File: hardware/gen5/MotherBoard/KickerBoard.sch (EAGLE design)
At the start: 154 parts, among them U1 SAM3S4B

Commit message: More Motherboard layout progress
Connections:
- removed net M0QA: U1.PA30
- removed net M0QB: U1.PA29
- removed net M1QA: U1.PA27
- removed net M1QB: U1.PA28
- removed net M2QA: U1.PA25
- removed net M2QB: U1.PA26
- removed net M3QA: U1.PA31
- removed net M3QB: U1.PA24
- net M1QA-1: now also U1.PA25
- net M1QA-2: now also U1.PA27
- net M1QA-3: now also U1.PA30
- net M1QA-4: now also U1.PA31
- net M1QB-1: now also U1.PA26
- net M1QB-2: now also U1.PA28
- net M1QB-3: now also U1.PA29
- net M1QB-4: now also U1.PA24
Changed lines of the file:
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@@
 <label x="495.3" y="137.16" size="1.778" layer="95"/>
+</segment>
+<segment>
+<pinref part="U1" gate="G$1" pin="PA24"/>
+<wire x1="746.76" y1="68.58" x2="746.76" y2="30.48" width="0.1524" layer="91"/>
+<label x="746.76" y="30.48" size="1.778" layer="95" rot="R90"/>
 </segment>
 </net>
@@
 <label x="495.3" y="142.24" size="1.778" layer="95"/>
 </segment>
+<segment>
+<pinref part="U1" gate="G$1" pin="PA31"/>
+<wire x1="762" y1="139.7" x2="762" y2="154.94" width="0.1524" layer="91"/>
+<wire x1="762" y1="154.94" x2="779.78" y2="154.94" width="0.1524" layer="91"/>
+<label x="774.7" y="154.94" size="1.778" layer="95"/>
+</segment>
 </net>
 <net name="M1QB-3" class="0">
@@
 <label x="414.02" y="137.16" size="1.778" layer="95"/>
 </segment>
+<segment>
+<pinref part="U1" gate="G$1" pin="PA29"/>
+<wire x1="784.86" y1="106.68" x2="812.8" y2="106.68" width="0.1524" layer="91"/>
+<label x="807.72" y="106.68" size="1.778" layer="95"/>
+</segment>
 </net>
 <net name="M1QA-3" class="0">
@@
 <label x="414.02" y="142.24" size="1.778" layer="95"/>
 </segment>
+<segment>
+<pinref part="U1" gate="G$1" pin="PA30"/>
+<wire x1="784.86" y1="109.22" x2="812.8" y2="109.22" width="0.1524" layer="91"/>
+<label x="807.72" y="109.22" size="1.778" layer="95"/>
+</segment>
 </net>
 <net name="M1QB-2" class="0">
@@
 <label x="335.28" y="137.16" size="1.778" layer="95"/>
 </segment>
+<segment>
+<pinref part="U1" gate="G$1" pin="PA28"/>
+<wire x1="784.86" y1="99.06" x2="812.8" y2="99.06" width="0.1524" layer="91"/>
+<label x="807.72" y="99.06" size="1.778" layer="95"/>
+</segment>
 </net>
 <net name="M1QA-2" class="0">
@@
 <label x="335.28" y="142.24" size="1.778" layer="95"/>
 </segment>
+<segment>
+<pinref part="U1" gate="G$1" pin="PA27"/>
+<wire x1="784.86" y1="96.52" x2="812.8" y2="96.52" width="0.1524" layer="91"/>
+<label x="807.72" y="96.52" size="1.778" layer="95"/>
+</segment>
 </net>
 <net name="M1QB-1" class="0">
@@
 <label x="317.5" y="210.82" size="1.778" layer="95"/>
 </segment>
+<segment>
+<pinref part="U1" gate="G$1" pin="PA26"/>
+<wire x1="754.38" y1="68.58" x2="754.38" y2="30.48" width="0.1524" layer="91"/>
+<label x="754.38" y="30.48" size="1.778" layer="95" rot="R90"/>
+</segment>
 </net>
 <net name="M1QA-1" class="0">
@@
 <wire x1="332.74" y1="215.9" x2="312.42" y2="215.9" width="0.1524" layer="91"/>
 <label x="317.5" y="215.9" size="1.778" layer="95"/>
+</segment>
+<segment>
+<pinref part="U1" gate="G$1" pin="PA25"/>
+<wire x1="751.84" y1="68.58" x2="751.84" y2="30.48" width="0.1524" layer="91"/>
+<label x="751.84" y="30.48" size="1.778" layer="95" rot="R90"/>
 </segment>
 </net>
@@
 </segment>
 </net>
-<net name="M3QB" class="0">
-<segment>
-<pinref part="U1" gate="G$1" pin="PA24"/>
-<wire x1="746.76" y1="68.58" x2="746.76" y2="30.48" width="0.1524" layer="91"/>
-<label x="746.76" y="30.48" size="1.778" layer="95" rot="R90"/>
-</segment>
-</net>
-<net name="M2QA" class="0">
-<segment>
-<pinref part="U1" gate="G$1" pin="PA25"/>
-<wire x1="751.84" y1="68.58" x2="751.84" y2="30.48" width="0.1524" layer="91"/>
-<label x="751.84" y="30.48" size="1.778" layer="95" rot="R90"/>
-</segment>
-</net>
-<net name="M2QB" class="0">
-<segment>
-<pinref part="U1" gate="G$1" pin="PA26"/>
-<wire x1="754.38" y1="68.58" x2="754.38" y2="30.48" width="0.1524" layer="91"/>
-<label x="754.38" y="30.48" size="1.778" layer="95" rot="R90"/>
-</segment>
-</net>
-<net name="M1QA" class="0">
-<segment>
-<pinref part="U1" gate="G$1" pin="PA27"/>
-<wire x1="784.86" y1="96.52" x2="812.8" y2="96.52" width="0.1524" layer="91"/>
-<label x="807.72" y="96.52" size="1.778" layer="95"/>
-</segment>
-</net>
-<net name="M1QB" class="0">
-<segment>
-<pinref part="U1" gate="G$1" pin="PA28"/>
-<wire x1="784.86" y1="99.06" x2="812.8" y2="99.06" width="0.1524" layer="91"/>
-<label x="807.72" y="99.06" size="1.778" layer="95"/>
-</segment>
-</net>
-<net name="M0QA" class="0">
-<segment>
-<pinref part="U1" gate="G$1" pin="PA30"/>
-<wire x1="784.86" y1="109.22" x2="812.8" y2="109.22" width="0.1524" layer="91"/>
-<label x="807.72" y="109.22" size="1.778" layer="95"/>
-</segment>
-</net>
-<net name="M0QB" class="0">
-<segment>
-<pinref part="U1" gate="G$1" pin="PA29"/>
-<wire x1="784.86" y1="106.68" x2="812.8" y2="106.68" width="0.1524" layer="91"/>
-<label x="807.72" y="106.68" size="1.778" layer="95"/>
-</segment>
-</net>
-<net name="M3QA" class="0">
-<segment>
-<pinref part="U1" gate="G$1" pin="PA31"/>
-<wire x1="762" y1="139.7" x2="762" y2="154.94" width="0.1524" layer="91"/>
-<wire x1="762" y1="154.94" x2="779.78" y2="154.94" width="0.1524" layer="91"/>
-<label x="774.7" y="154.94" size="1.778" layer="95"/>
-</segment>
-</net>

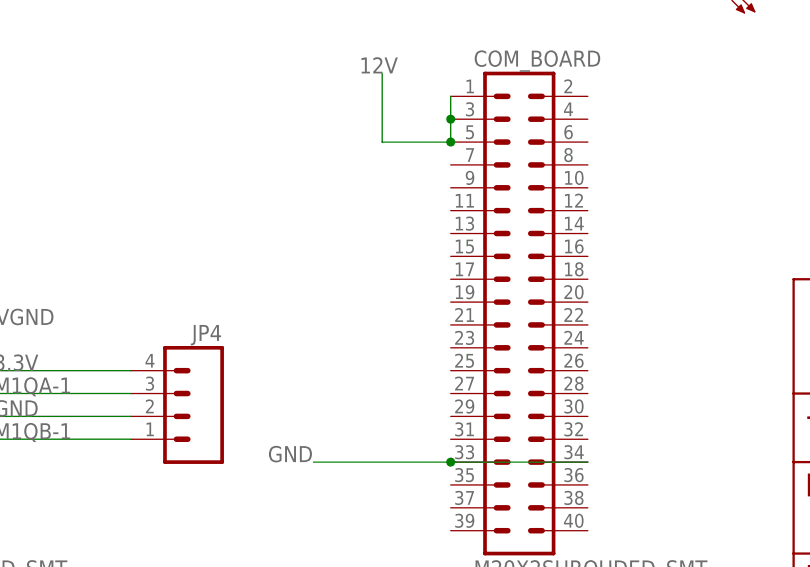
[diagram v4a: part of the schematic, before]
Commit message: Finishing up layout out traces for MCU on Motherboard
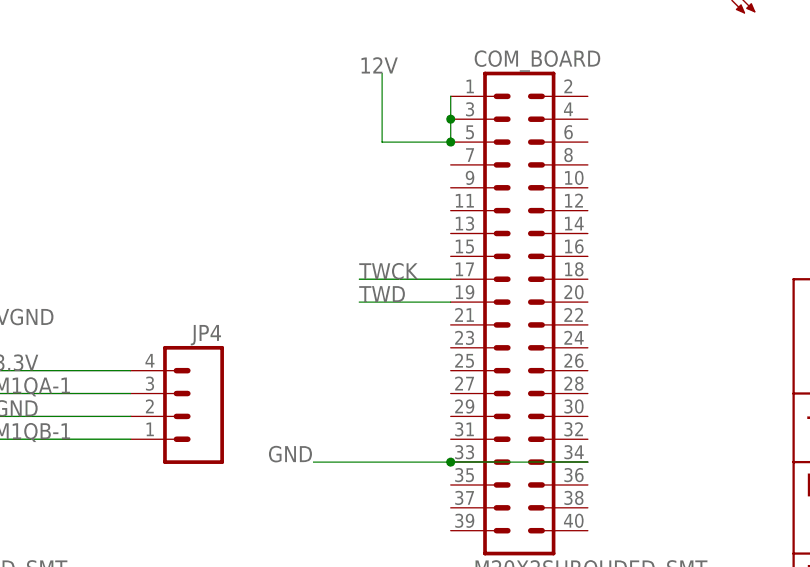
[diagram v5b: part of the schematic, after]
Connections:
- net TWCK: now also COM_BOARD.17
- net TWD: now also COM_BOARD.19
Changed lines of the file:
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@@
 <pinref part="R36" gate="G$1" pin="1"/>
+</segment>
+<segment>
+<pinref part="COM_BOARD" gate="G$1" pin="17"/>
+<wire x1="368.3" y1="228.6" x2="358.14" y2="228.6" width="0.1524" layer="91"/>
+<label x="358.14" y="228.6" size="1.778" layer="95"/>
 </segment>
 </net>
@@
 <pinref part="R35" gate="G$1" pin="1"/>
 </segment>
+<segment>
+<pinref part="COM_BOARD" gate="G$1" pin="19"/>
+<wire x1="368.3" y1="226.06" x2="358.14" y2="226.06" width="0.1524" layer="91"/>
+<label x="358.14" y="226.06" size="1.778" layer="95"/>
+</segment>
 </net>

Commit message: Motherboard Layout needs review, design rule checking, and new header for comms board. Other than that, the layout is done.
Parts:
- added U$19, U$20: INDUCTOR, gen3:INDUCTOR
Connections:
- new net N$28: MOTOR2.15, MOTOR2.16, MOTOR2.17, MOTOR2.18, U$8.P$5, U$8.P$6
- net 12V: now also PW_LED1.A
- net 12VGND: now also BATCLAMP2.A, R18.1, R21.1, U$19.P$1, U$20.P$1, U$8.P$7; no longer 3.3REG1.GND, C11.2, C8.2, C9.2, MOTOR2.15, MOTOR2.16, MOTOR2.17, MOTOR2.18, U$8.P$5, U$8.P$6
- net 3.3V: no longer MOTOR1.26, MOTOR2.26, MOTOR3.26, MOTOR4.26, PW_LED1.A
- net GND: now also 3.3REG1.GND, C11.2, C8.2, C9.2, U$19.P$2, U$20.P$2; no longer BATCLAMP2.A, MOTOR1.30, MOTOR2.30, MOTOR3.30, MOTOR4.30, R18.1, R21.1, U$8.P$7
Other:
- note added: "P8, P9, P10 are for Hall Sensors outputs... needed for proper operation of motor controller"

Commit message: Working through DRC Errors. Need to look into tolerances of PCB fab.
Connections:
- removed net N$34: C22.1, C24.1, C25.1, U1.VDDIN
- net 3.3V: now also C22.1, C24.1, C25.1, U1.VDDIN
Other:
- note removed: "DISCHARGE"

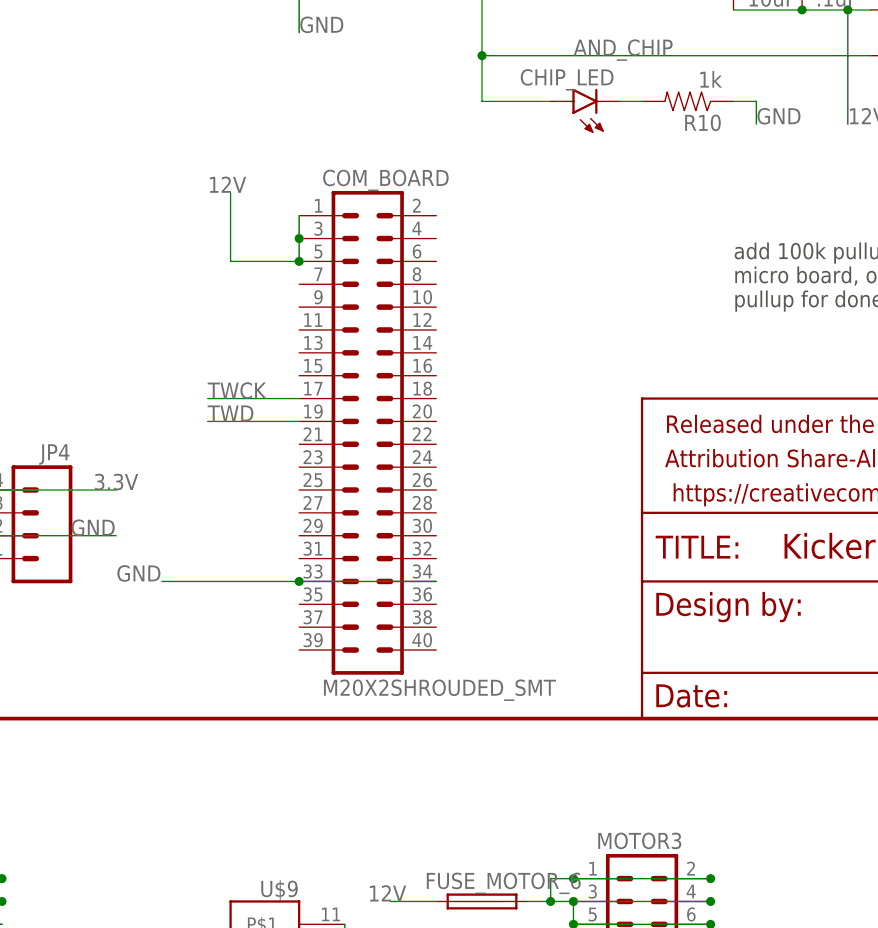
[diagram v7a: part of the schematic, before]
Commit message: Added the appropriate headers to the mother board
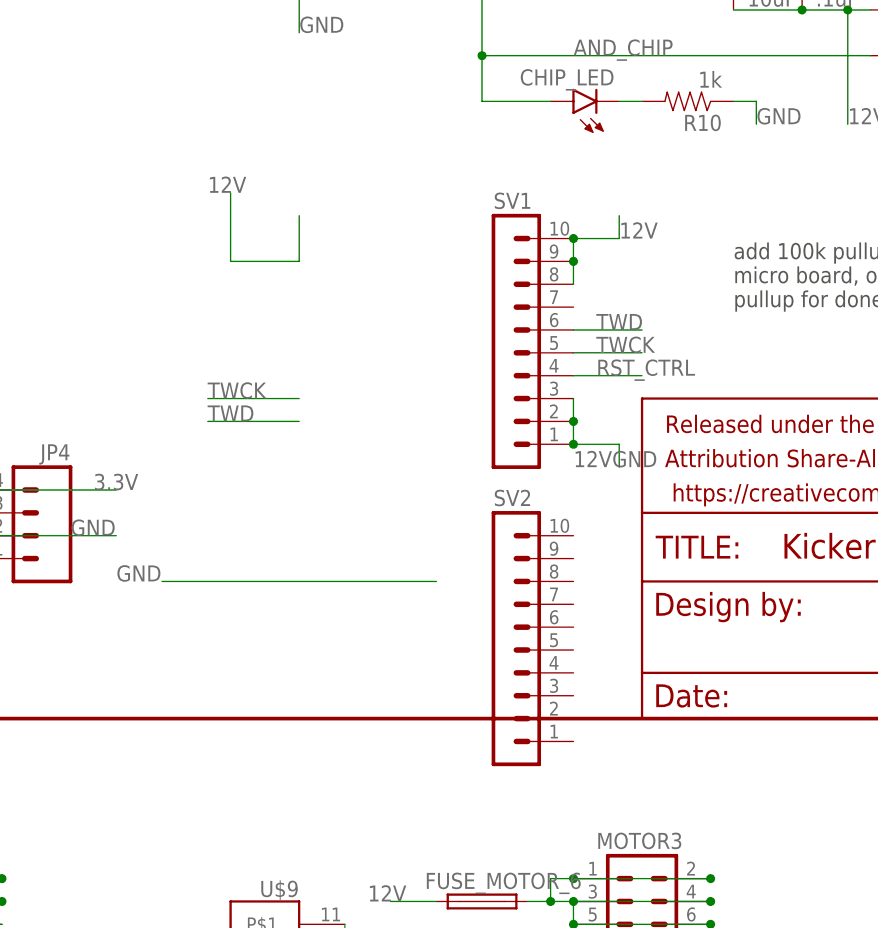
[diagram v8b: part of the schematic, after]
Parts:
- removed COM_BOARD: M20X2SHROUDED_SMT, SparkFun-Connectors:M20X2SHROUDED_SMT
- added SV1, SV2: (no value), con-lstb:MA10-1W
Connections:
- new net RST_CTRL: SV1.4
- net 12V: now also SV1.10, SV1.8, SV1.9; no longer COM_BOARD.1, COM_BOARD.3, COM_BOARD.5
- net 12VGND: now also SV1.1, SV1.2, SV1.3
- net GND: no longer COM_BOARD.33, COM_BOARD.34
- net TWCK: now also SV1.5; no longer COM_BOARD.17
- net TWD: now also SV1.6; no longer COM_BOARD.19
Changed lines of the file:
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@@
 <part name="MOTOR3" library="SparkFun-Connectors" deviceset="M20X2" device="SHROUDED_SMT"/>
 <part name="MOTOR4" library="SparkFun-Connectors" deviceset="M20X2" device="SHROUDED_SMT"/>
-<part name="COM_BOARD" library="SparkFun-Connectors" deviceset="M20X2" device="SHROUDED_SMT"/>
 <part name="KICKER1" library="fuse" deviceset="TR5" device=""/>
 <part name="U$2" library="rfc" deviceset="IXTA3N50D2" device=""/>
@@
 <part name="U$19" library="gen3" deviceset="INDUCTOR" device=""/>
 <part name="U$20" library="gen3" deviceset="INDUCTOR" device=""/>
+<part name="SV1" library="con-lstb" deviceset="MA10-1W" device=""/>
+<part name="SV2" library="con-lstb" deviceset="MA10-1W" device=""/>
 </parts>
 <sheets>
@@
 <instance part="MOTOR3" gate="G$1" x="406.4" y="152.4"/>
 <instance part="MOTOR4" gate="G$1" x="485.14" y="152.4"/>
-<instance part="COM_BOARD" gate="G$1" x="375.92" y="226.06"/>
 <instance part="KICKER1" gate="1" x="617.22" y="335.28" smashed="yes">
 <attribute name="NAME" x="610.87" y="336.677" size="1.778" layer="95"/>
@@
 <instance part="U$19" gate="G$1" x="490.22" y="370.84" rot="R270"/>
 <instance part="U$20" gate="G$1" x="495.3" y="370.84" rot="R270"/>
+<instance part="SV1" gate="1" x="391.16" y="233.68"/>
+<instance part="SV2" gate="1" x="391.16" y="200.66"/>
 </instances>
 <busses>
@@
 <segment>
 <label x="347.98" y="208.28" size="1.778" layer="95"/>
-<wire x1="353.06" y1="208.28" x2="368.3" y2="208.28" width="0.1524" layer="91"/>
-<pinref part="COM_BOARD" gate="G$1" pin="33"/>
 <label x="518.16" y="317.5" size="1.778" layer="95"/>
-<pinref part="COM_BOARD" gate="G$1" pin="34"/>
-<wire x1="368.3" y1="208.28" x2="383.54" y2="208.28" width="0.1524" layer="91"/>
-<junction x="368.3" y="208.28"/>
+<wire x1="353.06" y1="208.28" x2="383.54" y2="208.28" width="0.1524" layer="91"/>
 </segment>
 <segment>
@@
 <label x="467.36" y="330.2" size="1.778" layer="95"/>
 </segment>
+<segment>
+<pinref part="SV1" gate="1" pin="3"/>
+<pinref part="SV1" gate="1" pin="2"/>
+<wire x1="398.78" y1="228.6" x2="398.78" y2="226.06" width="0.1524" layer="91"/>
+<pinref part="SV1" gate="1" pin="1"/>
+<wire x1="398.78" y1="226.06" x2="398.78" y2="223.52" width="0.1524" layer="91"/>
+<junction x="398.78" y="226.06"/>
+<wire x1="398.78" y1="223.52" x2="403.86" y2="223.52" width="0.1524" layer="91"/>
+<wire x1="403.86" y1="223.52" x2="403.86" y2="220.98" width="0.1524" layer="91"/>
+<junction x="398.78" y="223.52"/>
+<label x="398.78" y="220.98" size="1.778" layer="95"/>
+</segment>
 </net>
 <net name="COMP_OUT" class="0">
@@
 </segment>
 <segment>
-<pinref part="COM_BOARD" gate="G$1" pin="1"/>
-<pinref part="COM_BOARD" gate="G$1" pin="3"/>
-<wire x1="368.3" y1="248.92" x2="368.3" y2="246.38" width="0.1524" layer="91"/>
-<pinref part="COM_BOARD" gate="G$1" pin="5"/>
-<wire x1="368.3" y1="246.38" x2="368.3" y2="243.84" width="0.1524" layer="91"/>
-<junction x="368.3" y="246.38"/>
+<wire x1="368.3" y1="248.92" x2="368.3" y2="243.84" width="0.1524" layer="91"/>
 <wire x1="368.3" y1="243.84" x2="360.68" y2="243.84" width="0.1524" layer="91"/>
 <wire x1="360.68" y1="243.84" x2="360.68" y2="251.46" width="0.1524" layer="91"/>
-<junction x="368.3" y="243.84"/>
 <label x="358.14" y="251.46" size="1.778" layer="95"/>
 </segment>
@@
 <wire x1="472.44" y1="355.6" x2="472.44" y2="365.76" width="0.1524" layer="91"/>
 <label x="472.44" y="363.22" size="1.778" layer="95"/>
+</segment>
+<segment>
+<pinref part="SV1" gate="1" pin="10"/>
+<pinref part="SV1" gate="1" pin="9"/>
+<wire x1="398.78" y1="246.38" x2="398.78" y2="243.84" width="0.1524" layer="91"/>
+<pinref part="SV1" gate="1" pin="8"/>
+<wire x1="398.78" y1="243.84" x2="398.78" y2="241.3" width="0.1524" layer="91"/>
+<junction x="398.78" y="243.84"/>
+<wire x1="398.78" y1="246.38" x2="403.86" y2="246.38" width="0.1524" layer="91"/>
+<wire x1="403.86" y1="246.38" x2="403.86" y2="248.92" width="0.1524" layer="91"/>
+<junction x="398.78" y="246.38"/>
+<label x="403.86" y="246.38" size="1.778" layer="95"/>
 </segment>
 </net>
@@
 </segment>
 <segment>
-<pinref part="COM_BOARD" gate="G$1" pin="17"/>
 <wire x1="368.3" y1="228.6" x2="358.14" y2="228.6" width="0.1524" layer="91"/>
 <label x="358.14" y="228.6" size="1.778" layer="95"/>
+</segment>
+<segment>
+<pinref part="SV1" gate="1" pin="5"/>
+<wire x1="398.78" y1="233.68" x2="406.4" y2="233.68" width="0.1524" layer="91"/>
+<label x="401.32" y="233.68" size="1.778" layer="95"/>
 </segment>
 </net>
@@
 </segment>
 <segment>
-<pinref part="COM_BOARD" gate="G$1" pin="19"/>
 <wire x1="368.3" y1="226.06" x2="358.14" y2="226.06" width="0.1524" layer="91"/>
 <label x="358.14" y="226.06" size="1.778" layer="95"/>
+</segment>
+<segment>
+<pinref part="SV1" gate="1" pin="6"/>
+<wire x1="398.78" y1="236.22" x2="406.4" y2="236.22" width="0.1524" layer="91"/>
+<label x="401.32" y="236.22" size="1.778" layer="95"/>
 </segment>
 </net>
@@
 </segment>
 </net>
+<net name="RST_CTRL" class="0">
+<segment>
+<pinref part="SV1" gate="1" pin="4"/>
+<wire x1="398.78" y1="231.14" x2="406.4" y2="231.14" width="0.1524" layer="91"/>
+<label x="401.32" y="231.14" size="1.778" layer="95"/>
+</segment>
+</net>
